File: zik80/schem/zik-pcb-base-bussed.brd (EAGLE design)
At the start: 99 x 98.7 mm, 55 parts, among them IC1 7432N, IC2 7404N

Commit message: Working on base pcb .. nearly there, but last few traces will take hours..
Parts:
- moved C5 2.00 mm to (45.2, 54.6)
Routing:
- net +3V3: track 344.9 -> 346.9 mm
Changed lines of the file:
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@@
 <element name="C2" library="rcl" package="C025-025X050" value=".1uF" x="26.67" y="42.2275"/>
 <element name="C4" library="rcl" package="C025-025X050" value=".1uF" x="32.385" y="37.7825"/>
-<element name="C5" library="rcl" package="C025-025X050" value=".1uF" x="43.18" y="54.61"/>
+<element name="C5" library="rcl" package="C025-025X050" value=".1uF" x="45.18025" y="54.64175"/>
 <element name="C6" library="rcl" package="C025-025X050" value=".1uF" x="48.26" y="63.1825" rot="R90"/>
 <element name="C7" library="rcl" package="C025-025X050" value=".1uF" x="42.8625" y="67.31"/>
@@
 <contactref element="R13" pad="1"/>
 <contactref element="IC1" pad="14"/>
-<wire x1="36.81" y1="55.92" x2="40.6" y2="55.92" width="0.3048" layer="1"/>
-<wire x1="40.6" y1="55.92" x2="41.91" y2="54.61" width="0.3048" layer="1"/>
+<wire x1="36.81" y1="55.92" x2="42.632" y2="55.92" width="0.3048" layer="1"/>
 <wire x1="36.81" y1="60.92" x2="47.3475" y2="60.92" width="0.3048" layer="1"/>
 <wire x1="47.3475" y1="60.92" x2="48.26" y2="61.9125" width="0.3048" layer="1"/>
@@
 <wire x1="96.2025" y1="19.685" x2="95.5675" y2="20.32" width="0.3048" layer="16"/>
 <wire x1="95.5675" y1="20.32" x2="92.71" y2="20.32" width="0.3048" layer="16"/>
+<wire x1="42.632" y1="55.92" x2="43.91025" y2="54.64175" width="0.3048" layer="1"/>
 <wire x1="74.93" y1="91.44" x2="92.075" y2="88.9" width="0" layer="19" extent="1-1"/>
 <wire x1="54.61" y1="79.375" x2="59.69" y2="93.98" width="0" layer="19" extent="1-1"/>

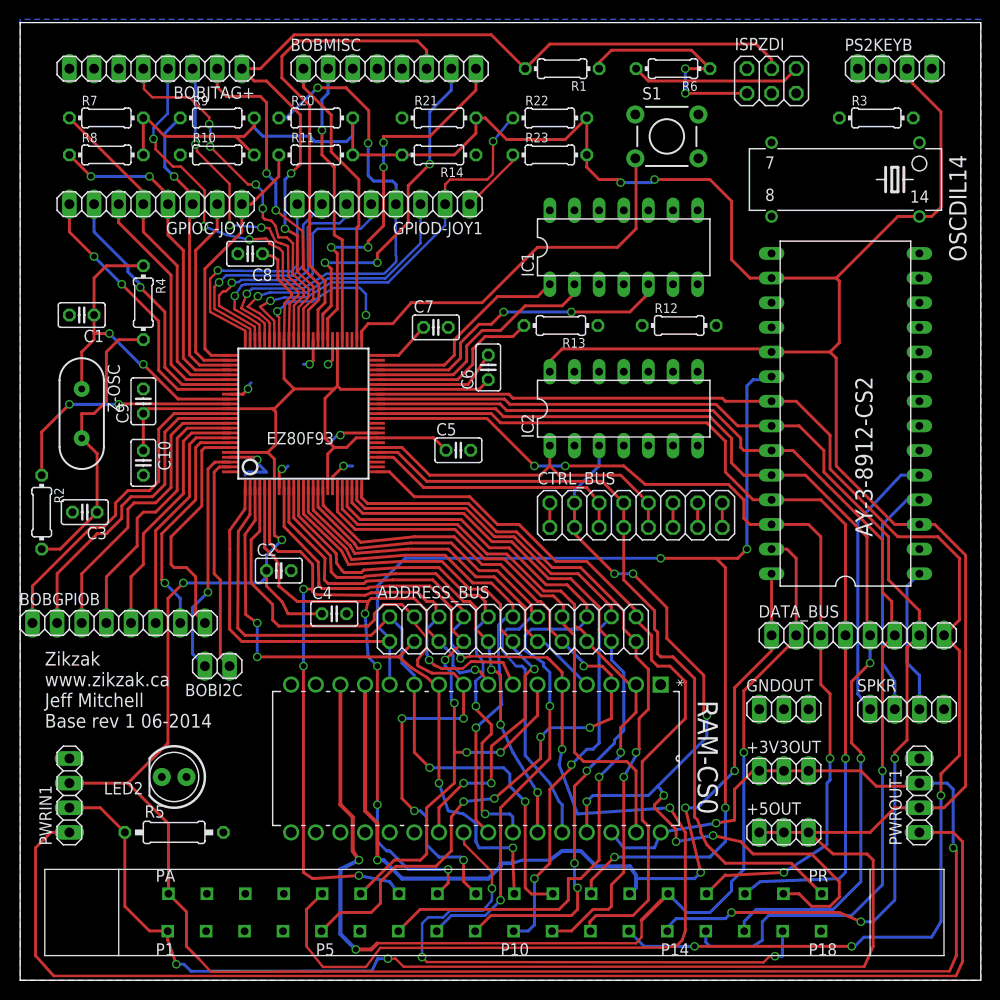
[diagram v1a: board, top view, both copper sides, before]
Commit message: Working on base pcb .. only about 20 more traces to go/cheat. Whew. Terrible mess, but maybe it'll work.. really needs larger pcb or more planes :O
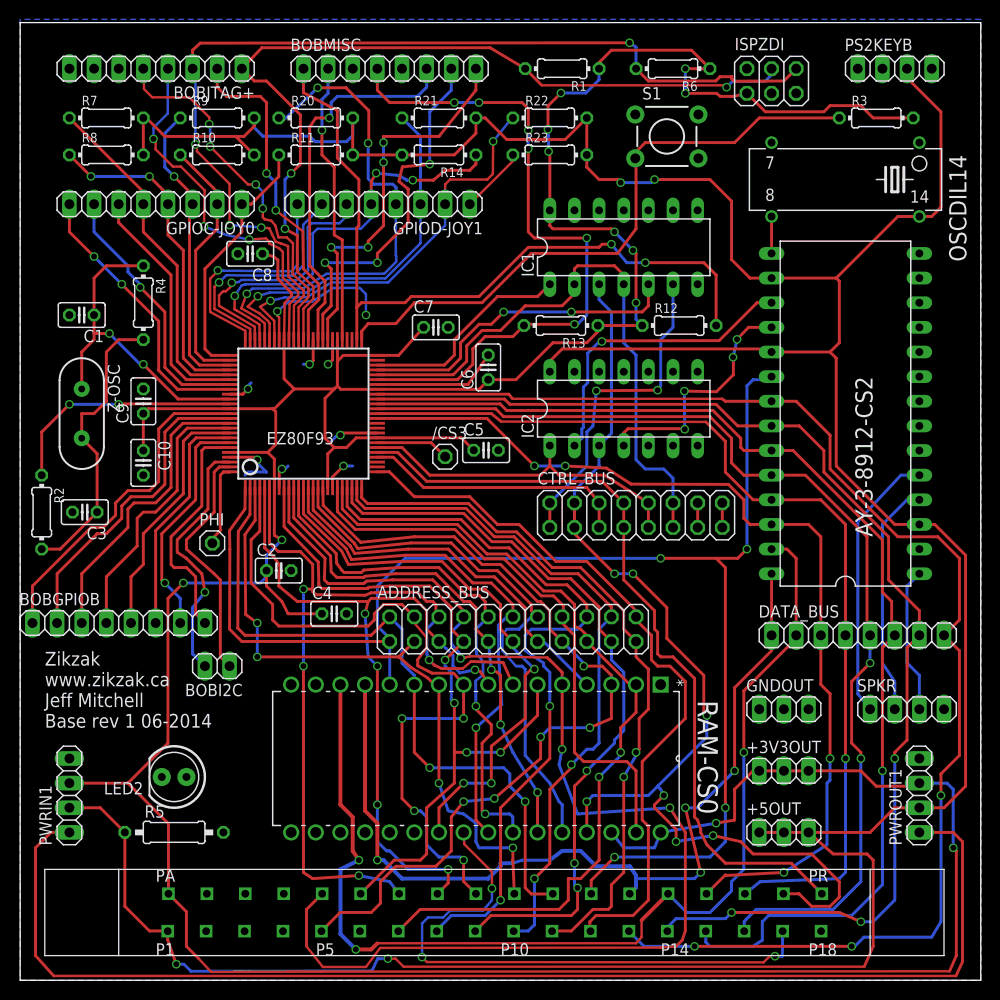
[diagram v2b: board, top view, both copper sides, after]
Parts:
- added /CS3, PHI: (no value), pinhead:1X01
- moved C5 2.86 mm to (48.0, 54.6)
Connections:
- net /CS3: now also /CS3.1; no longer BOBMISC.5
- net PHI: now also PHI.1; no longer BOBMISC.3
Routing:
- net +3V3: track 346.9 -> 429.2 mm, vias 6 -> 12
- net /IOREQ: track 18.4 -> 70.8 mm, vias 0 -> 6
- net TDI_ZDA: track 53.1 -> 103.8 mm, vias 3 -> 4
- net NMI: track 30.4 -> 77.4 mm, vias 0 -> 2
- net /MREQ: track 28.2 -> 62.1 mm
- net /MEMREAD: track 62.7 -> 93.9 mm, vias 3 -> 5
- net +CS2: track 0.00 -> 31.2 mm, vias 0 -> 1
- net +MEMWRITE: track 0.00 -> 25.3 mm, vias 0 -> 4
- net NRST: track 41.0 -> 64.3 mm
- net /MEMWRITE: track 90.4 -> 108.0 mm
- net PD4: track 27.3 -> 42.7 mm, vias 1 -> 3
- net RTC_VDD: track 49.3 -> 39.5 mm, vias 0 -> 1
- net PD2: track 28.9 -> 38.5 mm
- net PHI: track 0.00 -> 8.48 mm
- net /CS3: track 0.00 -> 7.60 mm
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
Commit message: zikzak base pcb rev1 sent to boardhouse :)
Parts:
- moved PS2KEYB 1.52 mm to (88.6, 94.0)
- moved LED2 1.27 mm to (17.1, 21.0)
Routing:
- net A9: track 55.7 -> 298.2 mm, vias 2 -> 10
- net D7: track 142.8 -> 325.4 mm, vias 3 -> 9
- net A12: track 39.6 -> 153.3 mm, vias 0 -> 2
- net A8: track 52.2 -> 160.4 mm, vias 3 -> 8
- net /MEMREAD: track 93.9 -> 200.3 mm
- net D4: track 109.1 -> 208.8 mm, vias 2 -> 7
- net PD6: track 24.8 -> 117.4 mm, vias 1 -> 2
- net D3: track 101.8 -> 187.4 mm, vias 1 -> 2
- net PD7: track 24.4 -> 101.9 mm, vias 1 -> 3
- net D2: track 98.0 -> 173.7 mm, vias 4 -> 5
- net D1: track 113.7 -> 188.7 mm, vias 3 -> 7
- net D0: track 93.0 -> 164.7 mm, vias 4 -> 7
- net /CS0: track 27.5 -> 97.3 mm, vias 0 -> 10
- net GND: track 41.2 -> 103.2 mm, vias 7 -> 15
- net /BUSACK: track 2.54 -> 60.3 mm, vias 0 -> 7
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- added copper zone on layer 1, net GND
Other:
- board text added: "1"
- board text added: "G"
